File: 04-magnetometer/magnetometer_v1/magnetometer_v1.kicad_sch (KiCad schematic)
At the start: 0 parts

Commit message: add magnetometer and can transceiver schematic
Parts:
- added C1, C7: 10nF, symbol Device:C
- added C10, C2: 1uF, symbol Device:C
- added C11, C6: 4.7uF, symbol Device:C
- added C12, C13, C14, C4, C5, C8, C9: 100nF, symbol Device:C
- added C15: 4.7nF, symbol Device:C
- added C3: 2.2uF, symbol Device:C
- added IC1: STM32F072CBT6, LQFP48-7x7mm, symbol 00-symbols:STM32F072CBT6
- added IC2: TMAG5170A1QDGKR, symbol 00-symbols:TMAG5170A1QDGKR
- added IC3: TCAN1042GVDRQ1, SOIC127P600X175-8N, symbol 00-symbols:TCAN1042GVDRQ1
- added J1: Conn_02x05_Odd_Even, symbol Connector_Generic:Conn_02x05_Odd_Even
- added R1: 10k, symbol Device:R
- added R2, R3: 62, symbol Device:R
- added U1: SPX3819M5-L-3-3/TR, symbol 00-symbols:SPX3819M5-L-3-3_TR
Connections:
- new net: C1.1, U1.4 (ADJ/BYP)
- new net: C15.1, R2.2, R3.2
- new net !CS: IC1.38 (PA15), IC2.4 (CS_N)
- new net 3v3: C10.2, C11.2, C12.2, C14.2, C3.1, C4.2, C5.2, C6.2, C7.2, C8.2, C9.2, IC1.1 (VBAT), IC1.24 (VDD), IC1.36 (VDDIO2), IC1.48 (VDD), IC1.9 (VDDA), IC2.5 (VCC), IC3.5 (VIO), J1.9 (Pin_9), U1.5 (VOUT)
- new net 5v: C13.2, C2.1, IC3.3 (VCC), J1.8 (Pin_8), U1.1 (VIN), U1.3 (EN)
- new net BOOT0: IC1.44 (BOOT0), J1.10 (Pin_10), R1.1
- new net CAN+: IC3.7 (CANH), J1.3 (Pin_3), J1.4 (Pin_4), R2.1
- new net CAN-: IC3.6 (CANL), J1.5 (Pin_5), J1.6 (Pin_6), R3.1
- new net GND: C1.2, C10.1, C11.1, C12.1, C13.1, C14.1, C15.2, C2.2, C3.2, C4.1, C5.1, C6.1, C7.1, C8.1, C9.1, IC1.23 (VSS), IC1.35 (VSS), IC1.47 (VSS), IC1.8 (VSSA), IC2.6 (GND), IC2.7 (TEST), IC3.2 (GND), IC3.8 (STB), J1.7 (Pin_7), R1.2, U1.2 (GND)
- new net MISO: IC1.16 (PA6), IC2.3 (MISO)
- new net MOSI: IC1.17 (PA7), IC2.2 (MOSI)
- new net SCLK: IC1.15 (PA5), IC2.1 (SCLK)
- new net USB_D+: J1.1 (Pin_1)
- new net USB_D-: J1.2 (Pin_2)
- new net can_rx: IC1.45 (PB8), IC3.4 (RXD)
- new net can_tx: IC1.46 (PB9), IC3.1 (TXD)
- no-connect marks 0 -> 31
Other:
- note added: "5v to 3v3 LDO"
- note added: "STM32F072CB and caps"
- note added: "can transceiver"
- note added: "connect pin 8 to stm gpio for low power sleep mode"
- note added: "magnetometer"
- note added: "pin 1, 48"
- note added: "pin 24"
- note added: "pin 36"
- note added: "pin 9"

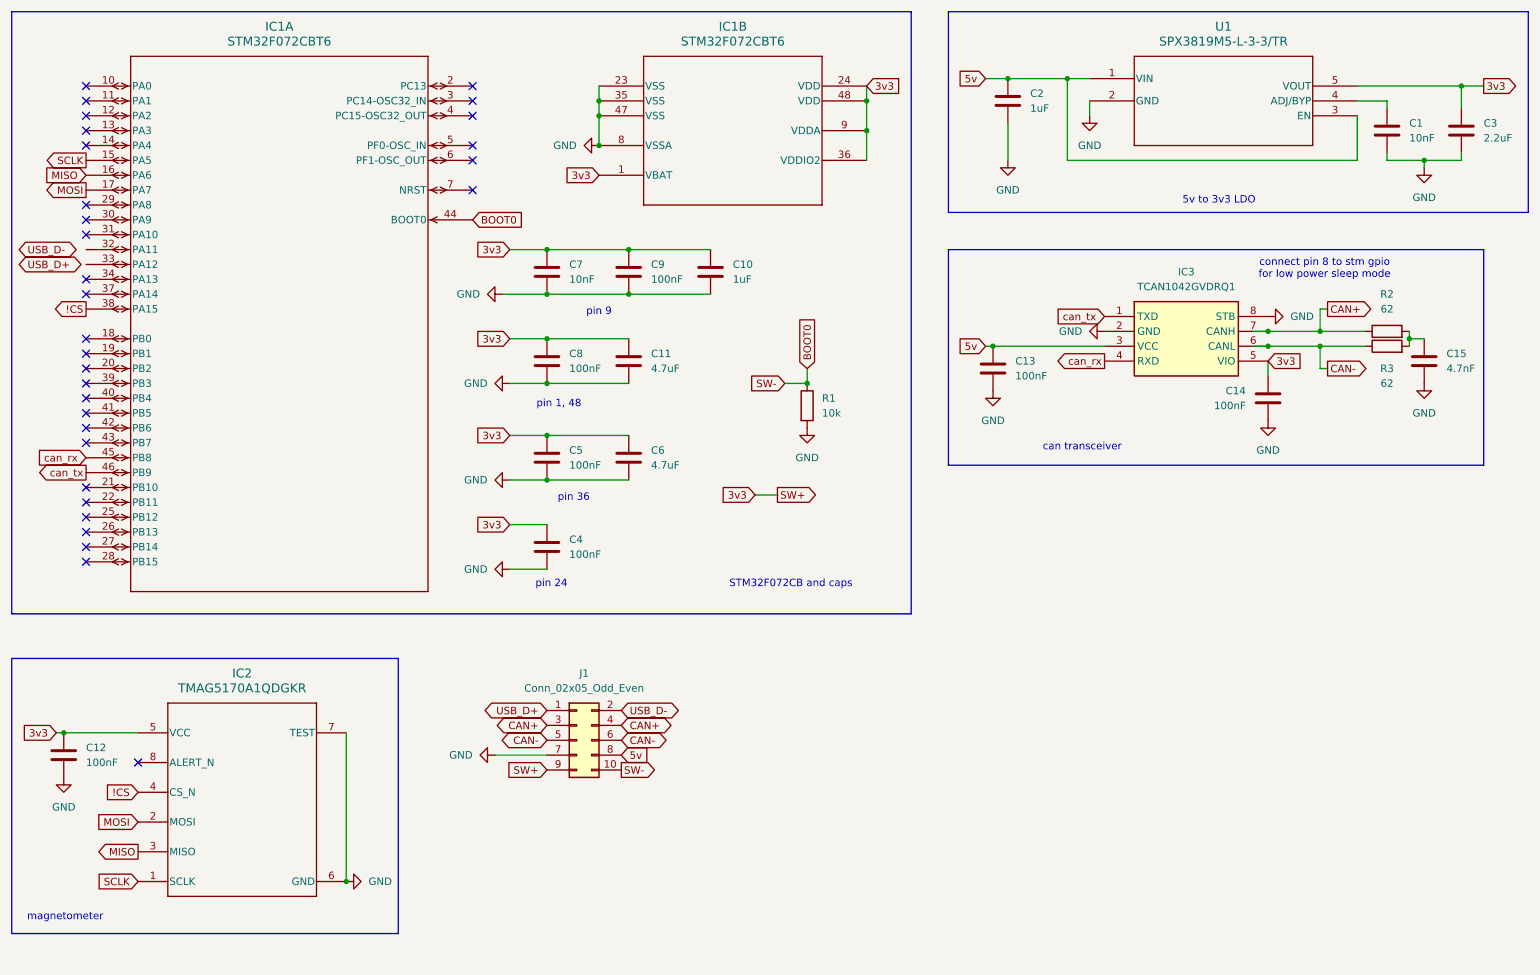
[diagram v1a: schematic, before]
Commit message: add usbc flash and boot/reset
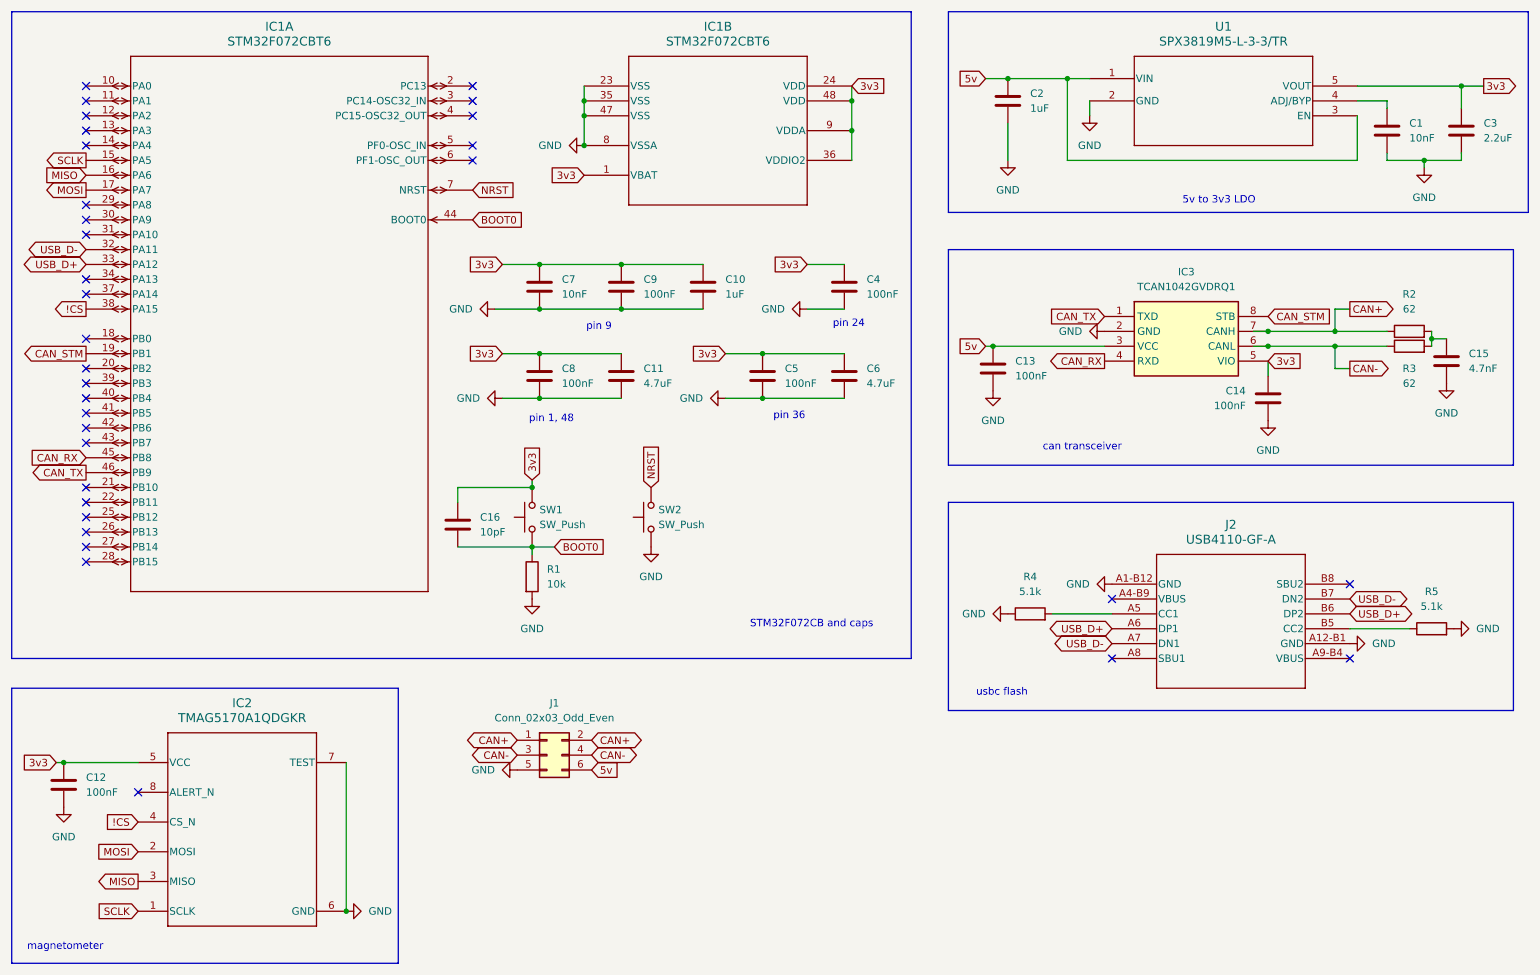
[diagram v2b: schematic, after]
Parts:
- removed J1: Conn_02x05_Odd_Even, symbol Connector_Generic:Conn_02x05_Odd_Even
- added C16: 10pF, symbol Device:C
- added J1: Conn_02x03_Odd_Even, symbol Connector_Generic:Conn_02x03_Odd_Even
- added J2: USB4110-GF-A, symbol 00-symbols:USB4110-GF-A
- added R4, R5: 5.1k, symbol Device:R
- added SW1, SW2: SW_Push, symbol Switch:SW_Push
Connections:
- net 3v3: now also C16.2, SW1.2
- net 5v: now also J1.6 (Pin_6)
- net BOOT0: now also C16.1, SW1.1
- net CAN+: now also J1.1 (Pin_1), J1.2 (Pin_2)
- net CAN-: now also J1.3 (Pin_3), J1.4 (Pin_4)
- net GND: now also J1.5 (Pin_5), J2.A1-B12 (GND), J2.A12-B1 (GND), R4.1, R5.2, SW2.1; no longer IC3.8 (STB)
- net USB_D+: now also IC1.33 (PA12), J2.A6 (DP1), J2.B6 (DP2)
- net USB_D-: now also IC1.32 (PA11), J2.A7 (DN1), J2.B7 (DN2)
- net CAN_STM: now reaches IC1.19 (PB1)
- net CAN_STM: now also IC3.8 (STB)
- net NRST: now reaches IC1.7 (NRST)
- net NRST: now also SW2.2
- net can_rx renamed CAN_RX
- net can_tx renamed CAN_TX
- new net: J2.A5 (CC1), R4.2
- new net: J2.B5 (CC2), R5.1
- no-connect marks 31 -> 33
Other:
- note added: "usbc flash"
- note removed: "connect pin 8 to stm gpio for low power sleep mode"
- moved on the sheet: C10, C11, C12, C15, C4, C5, C6, C7, C8, C9, IC1B, IC2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
